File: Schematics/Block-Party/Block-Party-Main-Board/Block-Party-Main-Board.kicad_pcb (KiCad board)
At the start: 2 copper layers, 190 x 160 mm, 28 parts, among them U1 ESP32-S3-DEVKITC-1-N8R2

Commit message: Added a usb power connector.
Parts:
- added J10: UJC-HP-3-SMT-TR, UJC-HP-3-SMT-TR:CUI_UJC-HP-3-SMT-TR, F.Cu at (289.1, 201.5)
- added R11: 5.1k, Resistor_SMD:R_0805_2012Metric, F.Cu at (287.3, 196.5)
- added R12: 5.1k, Resistor_SMD:R_0805_2012Metric, F.Cu at (290.6, 196.5)
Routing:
- net +5V: track 620.4 -> 685.3 mm
- net Net-(J10-CC1): track 0.00 -> 4.60 mm
- net Net-(J10-CC2): track 0.00 -> 4.49 mm

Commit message: Revision 1.01 of the PCBs
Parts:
- added J11: 691214110002S, 2p 3:691214110002S, F.Cu at (299.7, 126.4)
- added TP1: TestPoint, TestPoint:TestPoint_Pad_D2.0mm, F.Cu at (273.0, 50.2)
- added TP2: 5V, TestPoint:TestPoint_Pad_D2.0mm, F.Cu at (299.5, 137.2)
- added TP3: GND, TestPoint:TestPoint_Pad_D2.0mm, F.Cu at (295.0, 137.2)
- added TP4: TestPoint, TestPoint:TestPoint_Pad_D2.0mm, F.Cu at (244.5, 49.7)
- added TP5: TestPoint, TestPoint:TestPoint_Pad_D2.0mm, F.Cu at (244.5, 56.2)
- added TP6: TestPoint, TestPoint:TestPoint_Pad_D2.0mm, F.Cu at (256.0, 86.7)
- added TP7: TestPoint, TestPoint:TestPoint_Pad_D2.0mm, F.Cu at (256.0, 91.7)
- J10: footprint UJC-HP-3-SMT-TR:CUI_UJC-HP-3-SMT-TR -> Quinn_lib:USB_C-0015IPX6-00
- moved R12 0.70 mm to (290.5, 195.8)
- moved R11 0.70 mm to (287.3, 195.8)
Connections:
- U1 pad J3_5: unconnected-(U1-GPIO2-PadJ3_5) -> Net-(U1-GPIO2)
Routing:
- net +5V: track 685.3 -> 728.9 mm, vias 10 -> 11
- net Net-(U1-GPIO2): track 0.00 -> 35.4 mm
- net DO2: track 79.2 -> 90.7 mm, vias 1 -> 2
- net DO1: track 128.9 -> 139.5 mm, vias 1 -> 2
- net SENSE2: track 111.5 -> 119.2 mm
- net DO3: track 25.0 -> 31.6 mm
- net DO4: track 142.1 -> 145.2 mm
- net DO6: track 43.4 -> 40.5 mm
- net SENSE9: track 114.4 -> 117.1 mm
- net SENSE8: track 170.5 -> 173.3 mm
- net SENSE7: track 227.0 -> 229.8 mm
- net DO8: track 179.9 -> 182.6 mm
- net SENSE3: track 61.2 -> 58.5 mm
- net DO5: track 90.2 -> 92.9 mm
- net SENSE6: track 71.6 -> 74.3 mm
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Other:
- board text added: "5V"
- board text added: "GND"

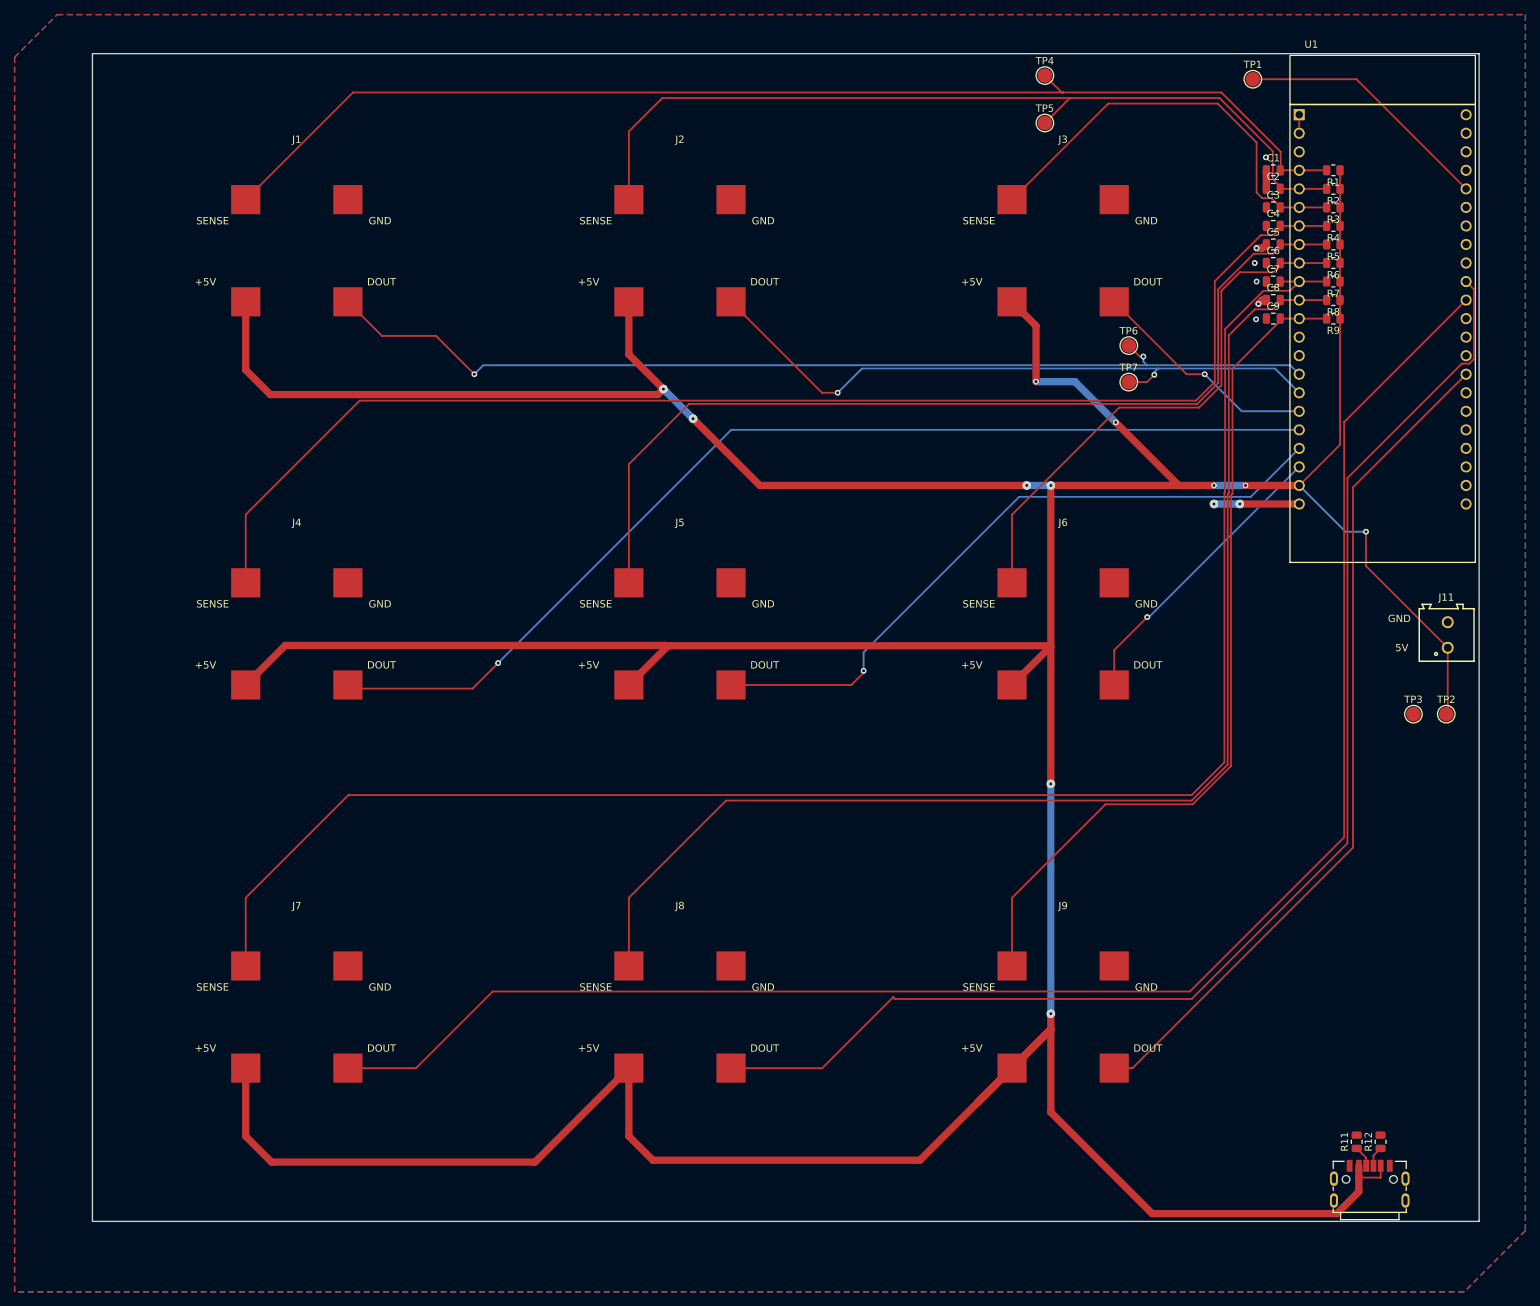
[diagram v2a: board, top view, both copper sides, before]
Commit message: Added main board mounting holes
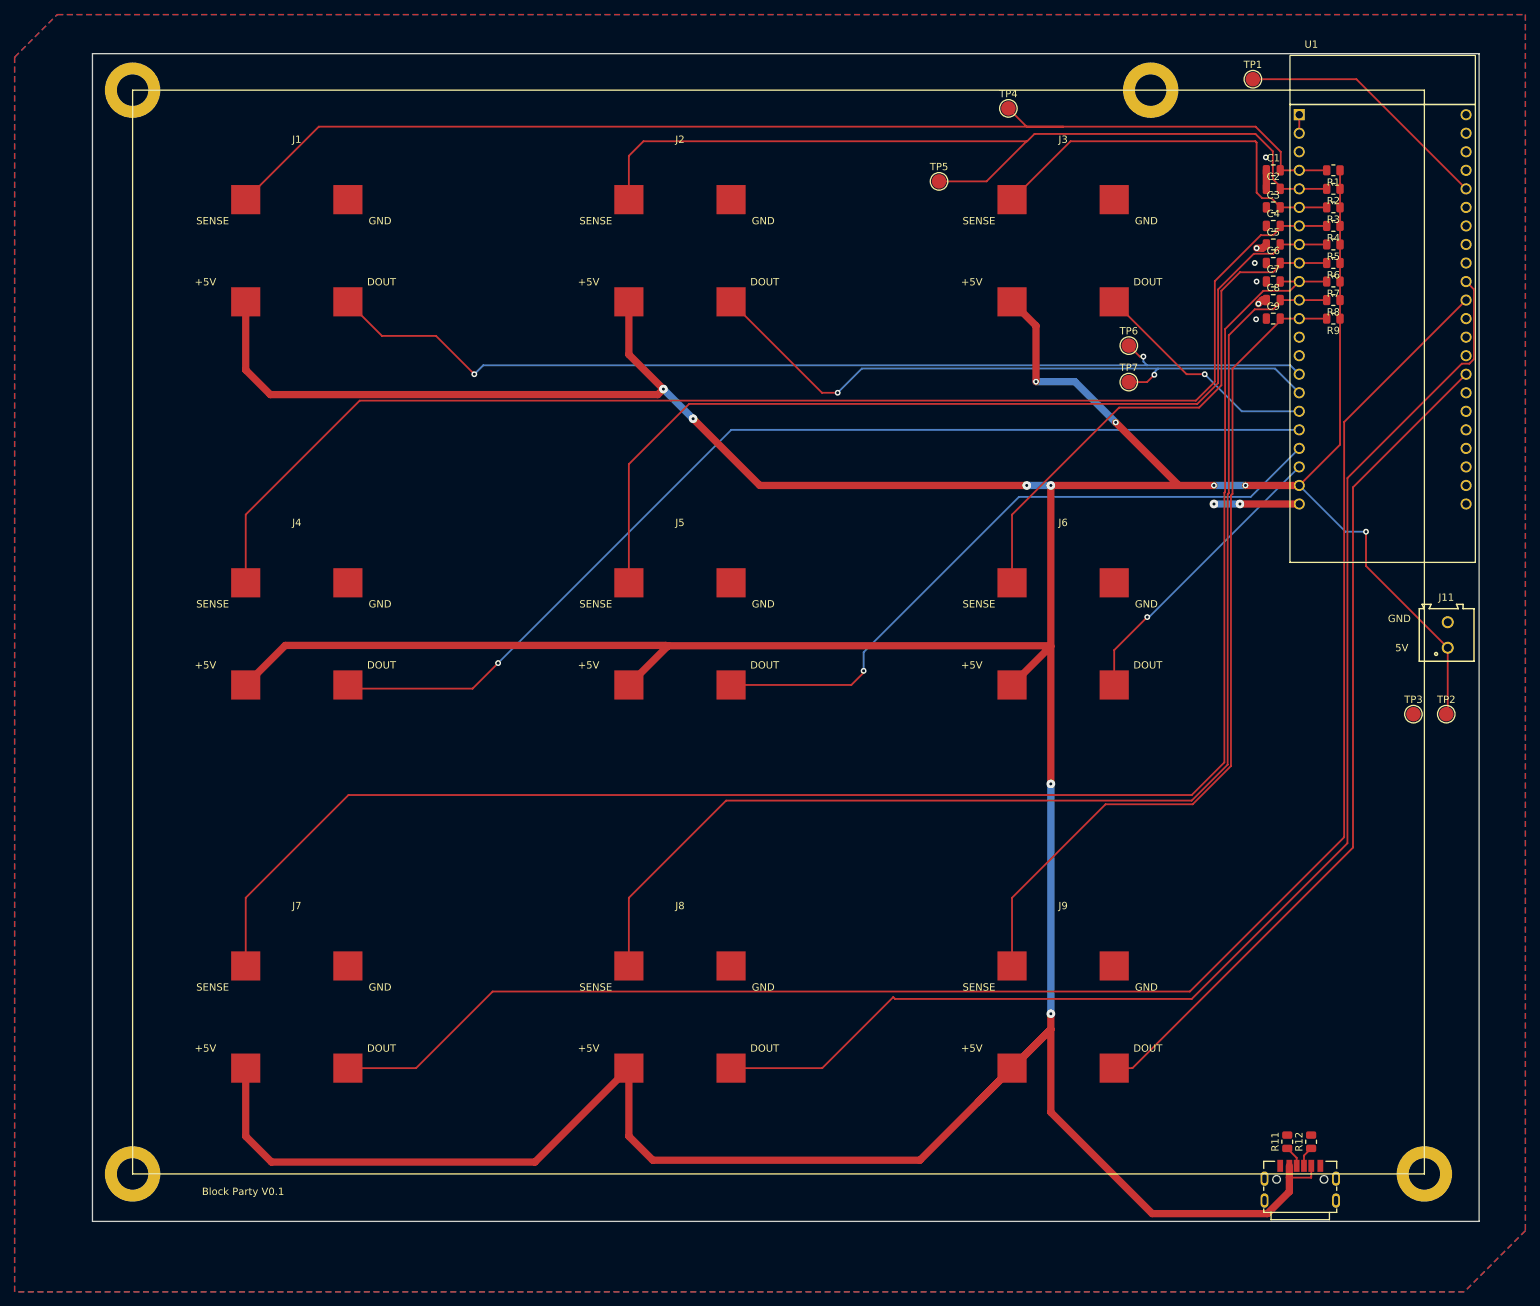
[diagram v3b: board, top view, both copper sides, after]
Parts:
- added REF**: MountingHole_4.3mm_M4_ISO7380_Pad, MountingHole:MountingHole_4.3mm_M4_ISO7380_Pad, F.Cu at (119.5, 200.2)
- added REF**: MountingHole_4.3mm_M4_ISO7380_Pad, MountingHole:MountingHole_4.3mm_M4_ISO7380_Pad, F.Cu at (259.0, 51.7)
- added REF**: MountingHole_4.3mm_M4_ISO7380_Pad, MountingHole:MountingHole_4.3mm_M4_ISO7380_Pad, F.Cu at (119.5, 51.7)
- added REF**: MountingHole_4.3mm_M4_ISO7380_Pad, MountingHole:MountingHole_4.3mm_M4_ISO7380_Pad, F.Cu at (296.5, 200.2)
- moved TP5 16.6 mm to (230.0, 64.2)
- moved J10 9.52 mm to (279.5, 201.5)
- moved R11 9.52 mm to (277.8, 195.8)
- moved R12 9.52 mm to (281.0, 195.8)
- moved TP4 6.73 mm to (239.5, 54.2)
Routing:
- net +5V: track 728.9 -> 719.4 mm
- net SENSE3: track 58.5 -> 54.2 mm
- net SENSE2: track 119.2 -> 122.6 mm
- net SENSE1: track 163.4 -> 164.6 mm
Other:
- board text added: "Block Party V0.1"

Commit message: Small tweaks and an update limiter for the esp32
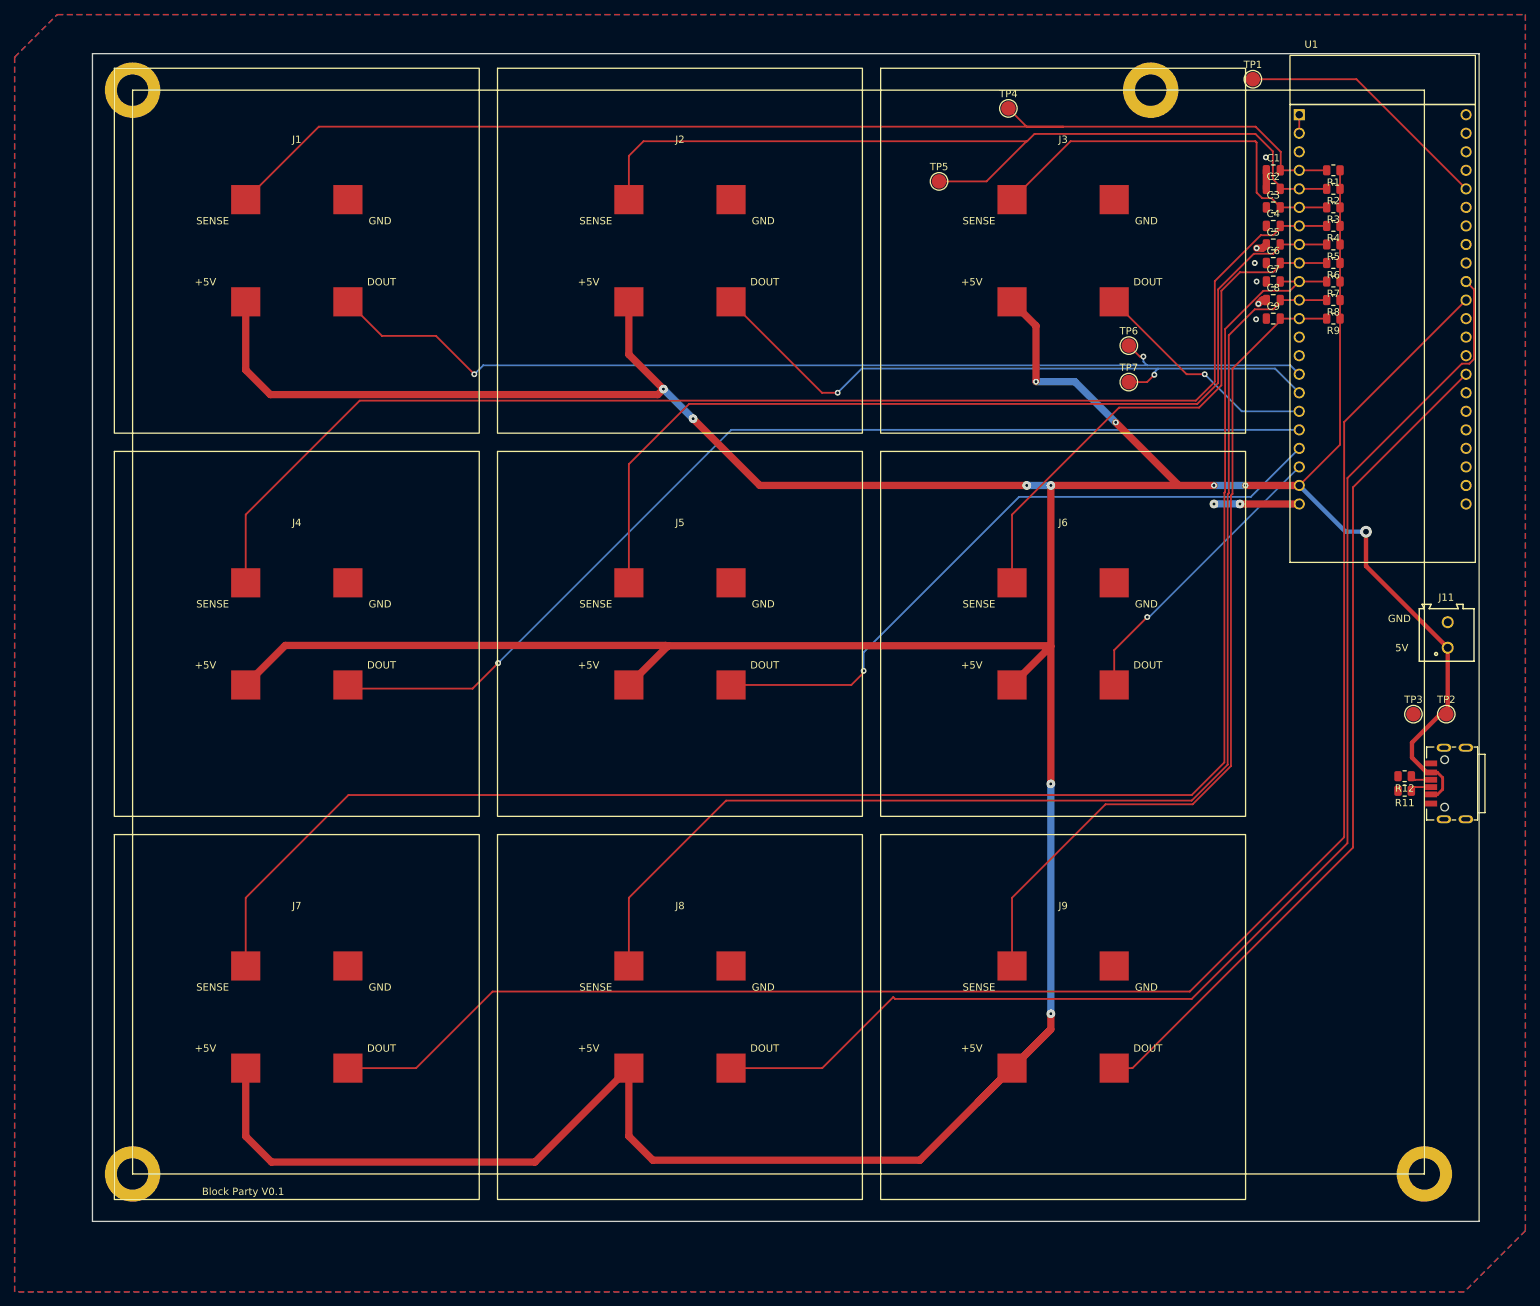
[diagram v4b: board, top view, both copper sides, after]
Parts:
- J10: value UJC-HP-3-SMT-TR -> USBC-0015IPX6-00
- TP2: value 5V -> TestPoint
- TP3: value GND -> TestPoint
- moved J10 58.4 mm to (299.8, 146.7), turned to 90 degrees
- moved R12 51.7 mm to (293.8, 145.7), turned to 180 degrees
- moved R11 50.7 mm to (293.8, 147.7), turned to 180 degrees
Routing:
- net +5V: track 719.4 -> 678.1 mm
